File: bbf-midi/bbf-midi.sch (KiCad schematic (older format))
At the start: 20 parts, among them J1 Conn_02x05_Odd_Even, J2 Conn_02x05_Odd_Even, J3 DIN-5_180degree, J4 DIN-5_180degree, J5 Conn_01x03, Q1 2N3904, U1 TLV1117-33, U2 H11L1

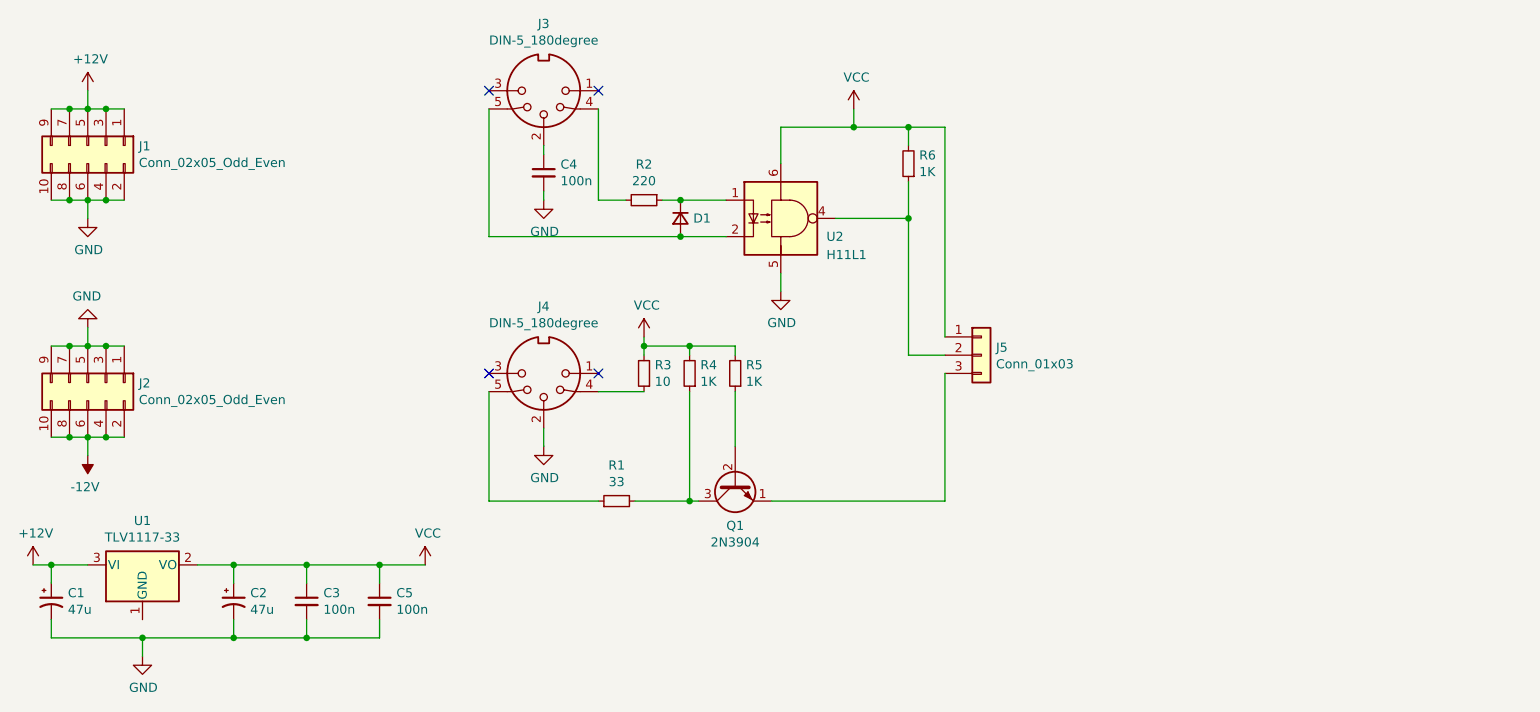
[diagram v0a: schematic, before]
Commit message: Fix some small mistakes in the midi friend.
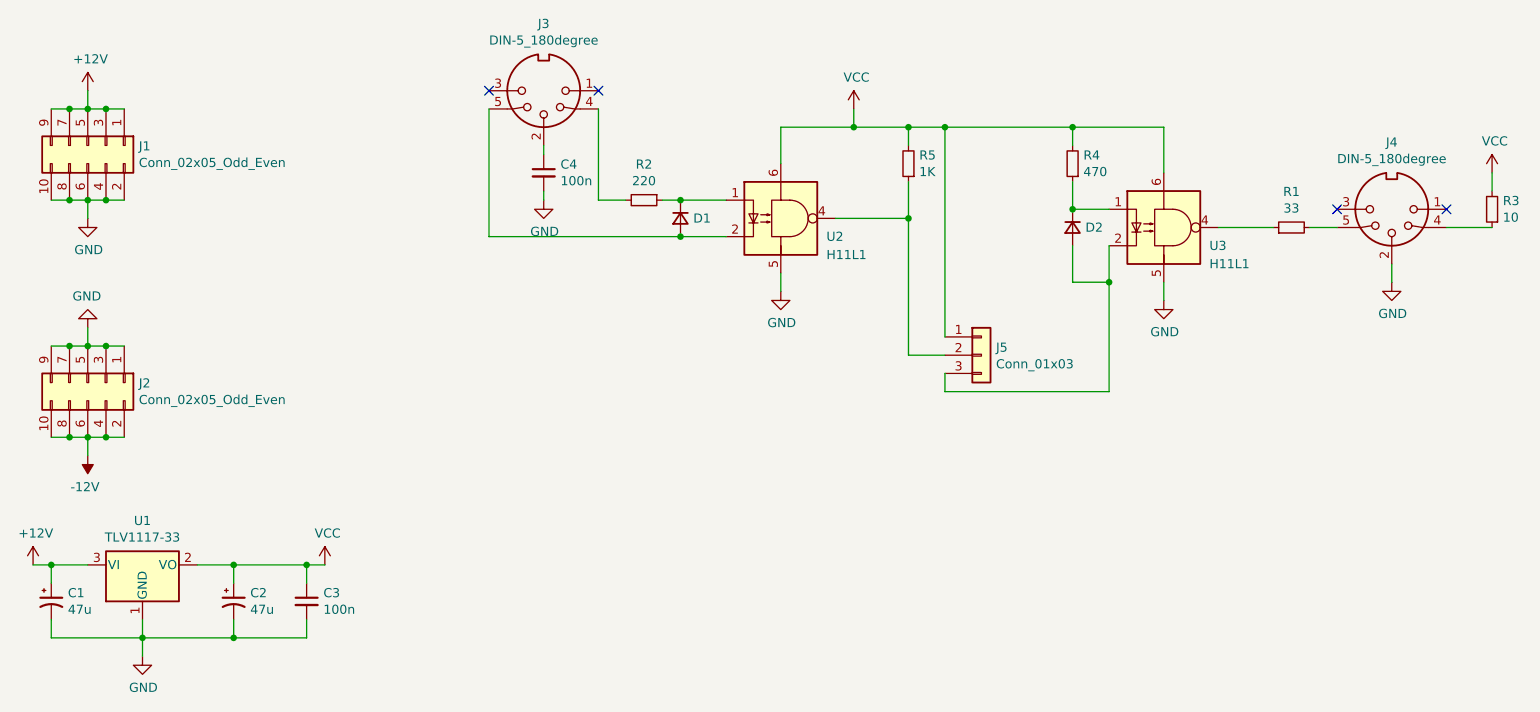
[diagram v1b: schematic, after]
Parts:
- removed C5: 100n, Capacitor_THT:C_Disc_D3.0mm_W2.0mm_P2.50mm, symbol Device:C_Small
- removed Q1: 2N3904, Package_TO_SOT_THT:TO-92_Inline, symbol Transistor_BJT:2N3904
- removed R5: 1K, Resistor_THT:R_Axial_DIN0207_L6.3mm_D2.5mm_P7.62mm_Horizontal, symbol Device:R_Small
- added D2: D_Small, Diode_THT:D_DO-35_SOD27_P7.62mm_Horizontal, symbol Device:D_Small
- added U3: H11L1, Package_DIP:DIP-6_W7.62mm_Socket, symbol Isolator:H11L1
- R4: value 1K -> 470
- renumbered R6 to R5
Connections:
- net GND: now also U1.1 (GND), U3.5
- net VCC: now also U3.6
- net at J4.5: now also R1.2; no longer R1.1
- net at J5.3 (Pin_3): now also D2.2 (A), U3.2
- net at R4.1: now also D2.1 (K), U3.1; no longer R1.2
- new net: R1.1, U3.4
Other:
- moved on the sheet: J4, R1, R3
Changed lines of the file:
@@
-$EndComp
-$Comp
-L Connector:DIN-5_180degree J4
-U 1 1 5F3FC648
-P 4500 3700
-F 0 "J4" H 4500 3333 50  0000 C CNN
-F 1 "DIN-5_180degree" H 4500 3424 50  0000 C CNN
-F 2 "davidstalnaker:DIN_5_CUI_SDF-50J" H 4500 3700 50  0001 C CNN
-F 3 "http://www.mouser.com/ds/2/18/40_c091_abd_e-75918.pdf" H 4500 3700 50  0001 C CNN
-	1    4500 3700
-	-1   0    0    1
 $EndComp
 $Comp
@@
 L power:VCC #PWR07
 U 1 1 5F4170AA
-P 3850 4750
-F 0 "#PWR07" H 3850 4600 50  0001 C CNN
-F 1 "VCC" H 3865 4923 50  0000 C CNN
-F 2 "" H 3850 4750 50  0001 C CNN
-F 3 "" H 3850 4750 50  0001 C CNN
-	1    3850 4750
+P 3300 4750
+F 0 "#PWR07" H 3300 4600 50  0001 C CNN
+F 1 "VCC" H 3315 4923 50  0000 C CNN
+F 2 "" H 3300 4750 50  0001 C CNN
+F 3 "" H 3300 4750 50  0001 C CNN
+	1    3300 4750
 	1    0    0    -1
 $EndComp
@@
 L power:GND #PWR09
 U 1 1 5F4216EB
-P 4500 4100
-F 0 "#PWR09" H 4500 3850 50  0001 C CNN
-F 1 "GND" H 4505 3927 50  0000 C CNN
-F 2 "" H 4500 4100 50  0001 C CNN
-F 3 "" H 4500 4100 50  0001 C CNN
-	1    4500 4100
-	1    0    0    -1
-$EndComp
-Wire Wire Line
-	4500 4100 4500 4000
+P 9150 3200
+F 0 "#PWR09" H 9150 2950 50  0001 C CNN
+F 1 "GND" H 9155 3027 50  0000 C CNN
+F 2 "" H 9150 3200 50  0001 C CNN
+F 3 "" H 9150 3200 50  0001 C CNN
+	1    9150 3200
+	1    0    0    -1
+$EndComp
+Wire Wire Line
+	9150 3200 9150 3100
 $Comp
 L power:GND #PWR08
@@
 NoConn ~ 4200 2150
 NoConn ~ 4800 2150
-NoConn ~ 4200 3700
-NoConn ~ 4800 3700
+NoConn ~ 8850 2800
+NoConn ~ 9450 2800
 Wire Wire Line
 	4800 2750 4950 2750
@@
 $EndComp
 $Comp
-L Device:R_Small R6
+L Device:R_Small R5
 U 1 1 5F43CF9F
 P 6500 2550
-F 0 "R6" H 6441 2504 50  0000 R CNN
+F 0 "R5" H 6441 2504 50  0000 R CNN
 F 1 "1K" H 6441 2595 50  0000 R CNN
 F 2 "Resistor_THT:R_Axial_DIN0207_L6.3mm_D2.5mm_P7.62mm_Horizontal" H 6500 2550 50  0001 C CNN
@@
 	6700 3500 6700 2350
 $Comp
-L power:VCC #PWR010
-U 1 1 5F44261C
-P 5050 3500
-F 0 "#PWR010" H 5050 3350 50  0001 C CNN
-F 1 "VCC" H 5065 3673 50  0000 C CNN
-F 2 "" H 5050 3500 50  0001 C CNN
-F 3 "" H 5050 3500 50  0001 C CNN
-	1    5050 3500
-	1    0    0    -1
-$EndComp
-$Comp
 L Device:R_Small R3
 U 1 1 5F442C9D
-P 5050 3700
-F 0 "R3" H 4991 3654 50  0000 R CNN
-F 1 "10" H 4991 3745 50  0000 R CNN
-F 2 "Resistor_THT:R_Axial_DIN0207_L6.3mm_D2.5mm_P7.62mm_Horizontal" H 5050 3700 50  0001 C CNN
-F 3 "~" H 5050 3700 50  0001 C CNN
-	1    5050 3700
-	-1   0    0    1
-$EndComp
-Wire Wire Line
-	5050 3500 5050 3550
-Wire Wire Line
-	4800 3800 5050 3800
+P 9700 2800
+F 0 "R3" H 9641 2754 50  0000 R CNN
+F 1 "10" H 9641 2845 50  0000 R CNN
+F 2 "Resistor_THT:R_Axial_DIN0207_L6.3mm_D2.5mm_P7.62mm_Horizontal" H 9700 2800 50  0001 C CNN
+F 3 "~" H 9700 2800 50  0001 C CNN
+	1    9700 2800
+	-1   0    0    1
+$EndComp
+Wire Wire Line
+	9450 2900 9700 2900
 Wire Wire Line
 	4800 2250 4800 2750
@@
 L Device:R_Small R1
 U 1 1 5F44BEF5
-P 4900 4400
-F 0 "R1" V 5096 4400 50  0000 C CNN
-F 1 "33" V 5005 4400 50  0000 C CNN
-F 2 "Resistor_THT:R_Axial_DIN0207_L6.3mm_D2.5mm_P7.62mm_Horizontal" H 4900 4400 50  0001 C CNN
-F 3 "~" H 4900 4400 50  0001 C CNN
-	1    4900 4400
+P 8600 2900
+F 0 "R1" V 8796 2900 50  0000 C CNN
+F 1 "33" V 8705 2900 50  0000 C CNN
+F 2 "Resistor_THT:R_Axial_DIN0207_L6.3mm_D2.5mm_P7.62mm_Horizontal" H 8600 2900 50  0001 C CNN
+F 3 "~" H 8600 2900 50  0001 C CNN
+	1    8600 2900
 	0    -1   -1   0
 $EndComp
-Wire Wire Line
-	4200 3800 4200 4400
-Wire Wire Line
-	4200 4400 4800 4400
 Wire Wire Line
 	1800 5150 2300 5150
@@
 	6500 2350 6700 2350
 Wire Wire Line
-	5750 4400 6700 4400
-Wire Wire Line
-	6700 3700 6700 4400
-Connection ~ 5050 3550
-Wire Wire Line
-	5050 3550 5050 3600
-Wire Wire Line
 	5800 2350 6200 2350
 Connection ~ 6200 2350
@@
 Wire Wire Line
 	3200 4850 3200 4750
-Connection ~ 3200 4750
-$Comp
-L Device:C_Small C5
-U 1 1 5F4D4F04
-P 3600 4950
-F 0 "C5" H 3692 4996 50  0000 L CNN
-F 1 "100n" H 3692 4905 50  0000 L CNN
-F 2 "Capacitor_THT:C_Disc_D3.0mm_W2.0mm_P2.50mm" H 3600 4950 50  0001 C CNN
-F 3 "~" H 3600 4950 50  0001 C CNN
-	1    3600 4950
-	1    0    0    -1
-$EndComp
-Wire Wire Line
-	3600 4750 3600 4850
-Wire Wire Line
-	3200 4750 3600 4750
-Wire Wire Line
-	3600 5050 3600 5150
-Wire Wire Line
-	3600 5150 3200 5150
-Connection ~ 3200 5150
-Wire Wire Line
-	3600 4750 3850 4750
-Connection ~ 3600 4750
 Wire Wire Line
 	2800 4750 3200 4750
@@
 Connection ~ 2800 5150
 $Comp
-L Transistor_BJT:2N3904 Q1
-U 1 1 5F48DEE4
-P 5550 4300
-F 0 "Q1" V 5785 4300 50  0000 C CNN
-F 1 "2N3904" V 5876 4300 50  0000 C CNN
-F 2 "Package_TO_SOT_THT:TO-92_Inline" H 5750 4225 50  0001 L CIN
-F 3 "https://www.fairchildsemi.com/datasheets/2N/2N3904.pdf" H 5550 4300 50  0001 L CNN
-	1    5550 4300
-	0    -1   1    0
-$EndComp
-$Comp
-L Device:R_Small R5
-U 1 1 5F4AADE9
-P 5550 3700
-F 0 "R5" H 5491 3654 50  0000 R CNN
-F 1 "1K" H 5491 3745 50  0000 R CNN
-F 2 "Resistor_THT:R_Axial_DIN0207_L6.3mm_D2.5mm_P7.62mm_Horizontal" H 5550 3700 50  0001 C CNN
-F 3 "~" H 5550 3700 50  0001 C CNN
-	1    5550 3700
-	-1   0    0    1
+L Isolator:H11L1 U3
+U 1 1 5F4CE214
+P 7900 2900
+F 0 "U3" H 8150 2800 50  0000 L CNN
+F 1 "H11L1" H 8150 2700 50  0000 L CNN
+F 2 "Package_DIP:DIP-6_W7.62mm_Socket" H 7810 2900 50  0001 C CNN
+F 3 "https://www.fairchildsemi.com/datasheets/H1/H11L1M.pdf" H 7810 2900 50  0001 C CNN
+	1    7900 2900
+	1    0    0    -1
 $EndComp
 $Comp
 L Device:R_Small R4
-U 1 1 5F4AA66C
-P 5300 3700
-F 0 "R4" H 5241 3654 50  0000 R CNN
-F 1 "1K" H 5241 3745 50  0000 R CNN
-F 2 "Resistor_THT:R_Axial_DIN0207_L6.3mm_D2.5mm_P7.62mm_Horizontal" H 5300 3700 50  0001 C CNN
-F 3 "~" H 5300 3700 50  0001 C CNN
-	1    5300 3700
-	-1   0    0    1
-$EndComp
-Wire Wire Line
-	5300 3800 5300 4400
-Wire Wire Line
-	5000 4400 5300 4400
-Wire Wire Line
-	5300 4400 5350 4400
-Connection ~ 5300 4400
-Wire Wire Line
-	5300 3600 5300 3550
-Wire Wire Line
-	5050 3550 5300 3550
-Connection ~ 5300 3550
-Wire Wire Line
-	5550 3800 5550 4100
-Wire Wire Line
-	5550 3600 5550 3550
-Wire Wire Line
-	5300 3550 5550 3550
+U 1 1 5F4CEA78
+P 7400 2550
+F 0 "R4" H 7341 2504 50  0000 R CNN
+F 1 "470" H 7341 2595 50  0000 R CNN
+F 2 "Resistor_THT:R_Axial_DIN0207_L6.3mm_D2.5mm_P7.62mm_Horizontal" H 7400 2550 50  0001 C CNN
+F 3 "~" H 7400 2550 50  0001 C CNN
+	1    7400 2550
+	-1   0    0    1
+$EndComp
+Wire Wire Line
+	8200 2900 8500 2900
+$Comp
+L power:VCC #PWR0101
+U 1 1 5F4E096D
+P 9700 2600
+F 0 "#PWR0101" H 9700 2450 50  0001 C CNN
+F 1 "VCC" H 9715 2773 50  0000 C CNN
+F 2 "" H 9700 2600 50  0001 C CNN
+F 3 "" H 9700 2600 50  0001 C CNN
+	1    9700 2600
+	1    0    0    -1
+$EndComp
+Wire Wire Line
+	9700 2600 9700 2700
+$Comp
+L power:GND #PWR0102
+U 1 1 5F4E291C
+P 7900 3300
+F 0 "#PWR0102" H 7900 3050 50  0001 C CNN
+F 1 "GND" H 7905 3127 50  0000 C CNN
+F 2 "" H 7900 3300 50  0001 C CNN
+F 3 "" H 7900 3300 50  0001 C CNN
+	1    7900 3300
+	1    0    0    -1
+$EndComp
+Wire Wire Line
+	7900 3200 7900 3300
+$Comp
+L Connector:DIN-5_180degree J4
+U 1 1 5F3FC648
+P 9150 2800
+F 0 "J4" H 9150 2433 50  0000 C CNN
+F 1 "DIN-5_180degree" H 9150 2524 50  0000 C CNN
+F 2 "davidstalnaker:DIN_5_CUI_SDF-50J" H 9150 2800 50  0001 C CNN
+F 3 "http://www.mouser.com/ds/2/18/40_c091_abd_e-75918.pdf" H 9150 2800 50  0001 C CNN
+	1    9150 2800
+	-1   0    0    1
+$EndComp
+Wire Wire Line
+	8700 2900 8850 2900
+Wire Wire Line
+	6700 2350 7400 2350
+Wire Wire Line
+	7400 2350 7400 2450
+Connection ~ 6700 2350
+Wire Wire Line
+	7400 2350 7900 2350
+Wire Wire Line
+	7900 2350 7900 2600
+Connection ~ 7400 2350
+Wire Wire Line
+	7400 2650 7400 2800
+Wire Wire Line
+	7400 2800 7600 2800
+Wire Wire Line
+	6700 3700 6700 3800
+Wire Wire Line
+	6700 3800 7600 3800
+Wire Wire Line
+	7600 3800 7600 3200
+$Comp
+L Device:D_Small D2
+U 1 1 5F51618A
+P 7400 2900
+F 0 "D2" V 7400 2970 50  0000 L CNN
+F 1 "D_Small" V 7445 2970 50  0001 L CNN
+F 2 "Diode_THT:D_DO-35_SOD27_P7.62mm_Horizontal" V 7400 2900 50  0001 C CNN
+F 3 "~" V 7400 2900 50  0001 C CNN
+	1    7400 2900
+	0    1    1    0
+$EndComp
+Connection ~ 7400 2800
+Wire Wire Line
+	7400 3000 7400 3200
+Wire Wire Line
+	7400 3200 7600 3200
+Connection ~ 7600 3200
+Wire Wire Line
+	7600 3200 7600 3000
+Wire Wire Line
+	3300 4750 3200 4750
+Connection ~ 3200 4750
+Wire Wire Line
+	2300 5050 2300 5150
 $EndSCHEMATC
